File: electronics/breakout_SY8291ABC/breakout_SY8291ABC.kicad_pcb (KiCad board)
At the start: 2 copper layers, 18.5 x 12.7 mm, 19 parts, among them J1 Conn_01x04, U1 SY8120

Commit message: modified, layedout, and completed, now wait one day in between
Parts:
- removed C2: 10u, SquantorRcl:C_1206_0805
- C4: value 47p -> 22p
- L1: value 4.7u -> TBD
- N1: value 20210414 -> 20210417
- R3: value 22K -> TBD
- U1: value SY8120 -> SY8291
- moved R5 1.80 mm to (150.4, 75.6), turned to 180 degrees
- moved N1 0.95 mm to (148.8, 71.3)
- moved C1 0.90 mm to (144.2, 75.0)
- moved C3 0.90 mm to (147.7, 72.0)
- moved C4 0.90 mm to (141.0, 68.5)
- moved L1 0.90 mm to (151.8, 70.4)
- moved R2 0.90 mm to (142.1, 68.5)
- moved U1 0.90 mm to (145.2, 71.7)
- moved C5 0.90 mm to (145.5, 67.8)
- moved C6 0.90 mm to (143.6, 67.8)
- moved C7 0.90 mm to (147.4, 67.8)
- moved R1 0.90 mm to (141.7, 71.1)
- moved R3 0.90 mm to (142.8, 71.1)
- moved R4 0.90 mm to (140.6, 71.1)
- moved D1 0.82 mm to (153.1, 75.6), turned to 180 degrees
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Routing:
- net /Vin: track 23.4 -> 17.4 mm, vias 6 -> 7
- net /Vout: track 45.1 -> 47.5 mm
- net Net-(D1-Pad2): track 2.71 -> 1.30 mm
- net /GND: track 5.62 -> 6.57 mm
- net /Enable: track 4.62 -> 5.52 mm
- added copper zone on B.Cu, net /Vin
- added copper zone on F.Cu, net /Vin
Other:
- board size 18.5 x 12.7 mm -> 18.5 x 10.7 mm

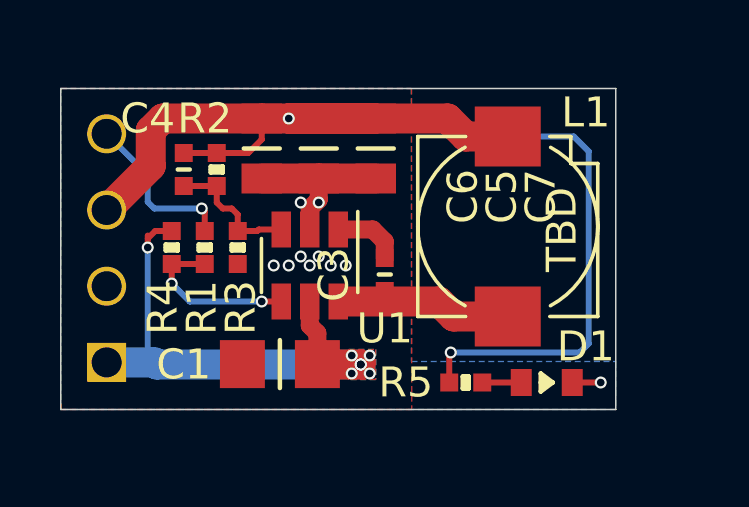
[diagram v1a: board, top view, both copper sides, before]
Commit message: added additional current label, optimized some track placement
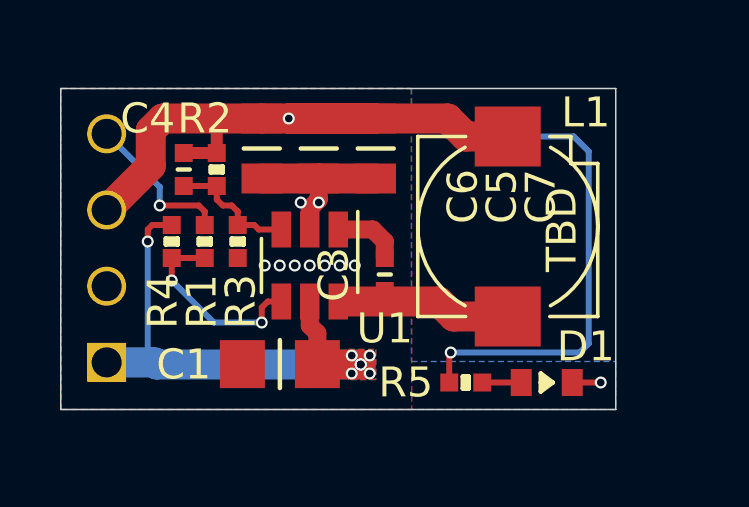
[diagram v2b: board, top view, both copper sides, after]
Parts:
- added N4: A:, SquantorLabels:Label_Note_medium, B.Cu at (150.1, 75.4)
- N1: value 20210417 -> 20210418
- N3: value Vout: -> V:
- moved N3 5.01 mm to (153.5, 69.4), turned to 270 degrees
- moved N2 1.27 mm to (144.1, 72.1)
- moved N1 1.10 mm to (147.7, 71.3)
- moved R1 0.20 mm to (141.7, 70.9)
- moved R3 0.20 mm to (142.8, 70.9)
- moved R4 0.20 mm to (140.6, 70.9)
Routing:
- net /Vout: track 47.5 -> 46.2 mm
- net Net-(R1-Pad1): track 5.65 -> 6.66 mm

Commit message: added soldermask keepout, DRC errors fixed, title added, changed Vout Iout labels
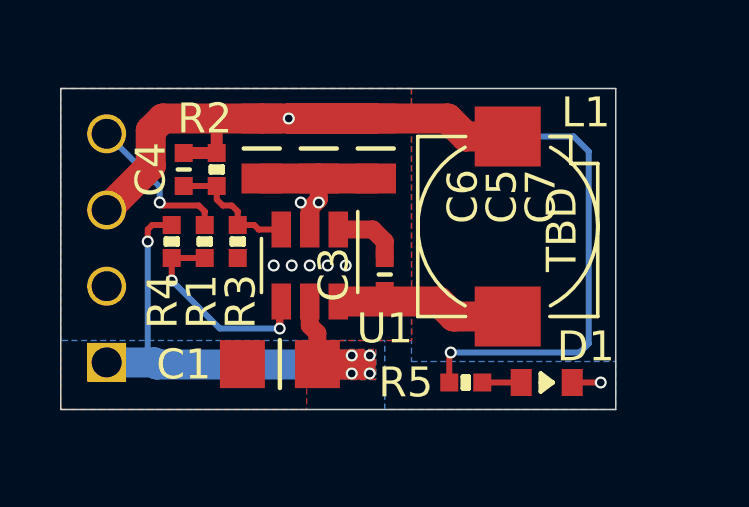
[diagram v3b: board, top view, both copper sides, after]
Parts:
- N1: value 20210418 -> 20210419
- moved N1 1.20 mm to (146.9, 70.4)
- moved N2 1.20 mm to (143.3, 71.2)
- moved N4 0.20 mm to (150.3, 75.4)
- moved N3 0.10 mm to (153.6, 69.4)
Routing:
- net /Vin: vias 7 -> 5
- net /GND: vias 10 -> 8
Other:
- board text added: "SY8291 40V 1.2A"

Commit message: changed indicator power led, changed inductor size, enlarged PCB a bit
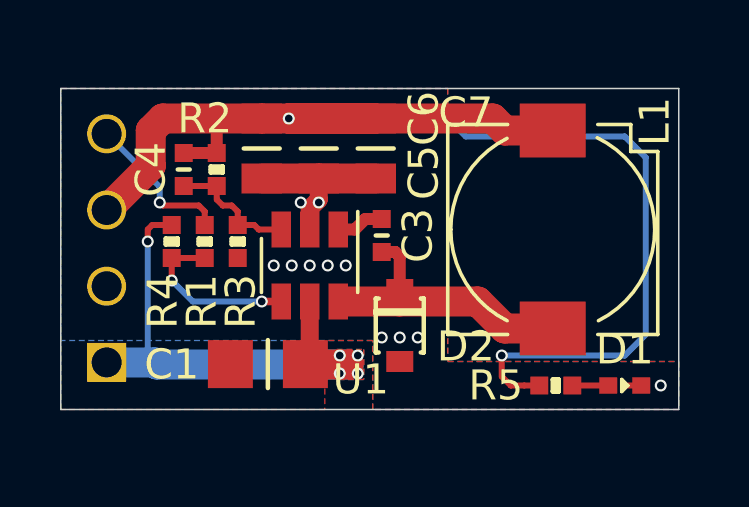
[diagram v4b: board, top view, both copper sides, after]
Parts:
- added D2: B140WS, SquantorDiodes:SOD_323_onsemi, F.Cu at (148.2, 73.7)
- D1: footprint SquantorDiodes:LED_0603_hand -> SquantorDiodes:LED_0402_osram
- L1: footprint SquantorRcl:L_SLF6045 -> SquantorRcl:L_SLF70XX_TDK_hand
- N1: value 20210419 -> 20210421
- moved R5 3.00 mm to (153.4, 75.7)
- moved D1 2.60 mm to (155.7, 75.7)
- moved L1 1.50 mm to (153.3, 70.5)
- moved C3 1.30 mm to (147.6, 70.7)
- moved C1 0.40 mm to (143.8, 75.0)
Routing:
- net /Vout: track 46.2 -> 50.5 mm
- net Net-(C3-Pad1): track 5.86 -> 9.68 mm
- net Net-(R1-Pad1): track 7.03 -> 5.79 mm
- net Net-(C3-Pad2): track 2.27 -> 1.59 mm
- net /GND: track 6.57 -> 6.27 mm, vias 8 -> 11
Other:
- board size 18.5 x 10.7 mm -> 20.6 x 10.7 mm

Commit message: updated versionnumber, changed coil sizes
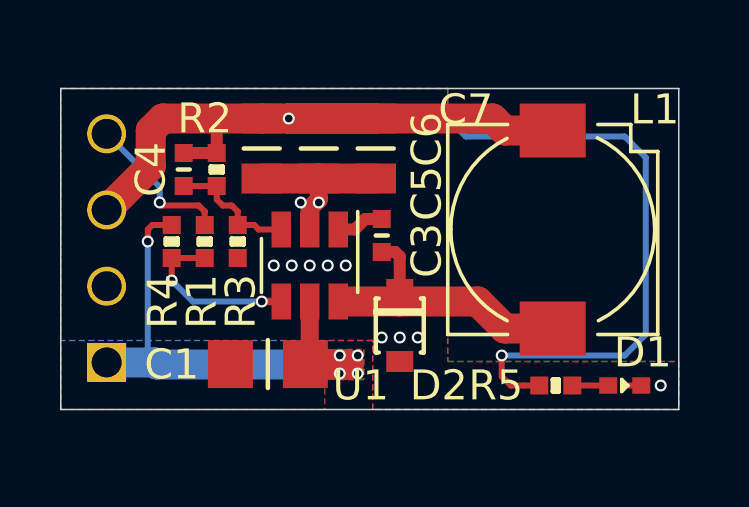
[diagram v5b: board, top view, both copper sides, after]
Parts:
- N1: value 20210421 -> 20210422
- moved N3 1.70 mm to (155.3, 69.4)
- moved N4 1.70 mm to (152.0, 75.4)
- moved N1 1.30 mm to (148.2, 70.4)
- moved N2 1.30 mm to (144.6, 71.2)

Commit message: minor silk updates, updated versionnumber
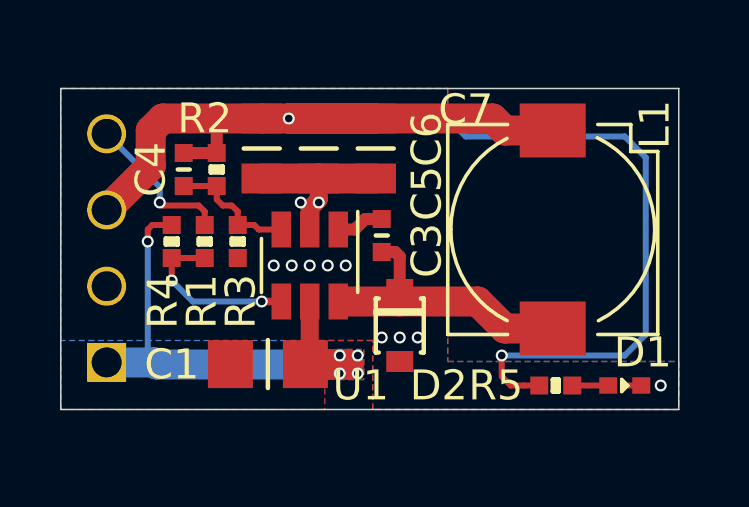
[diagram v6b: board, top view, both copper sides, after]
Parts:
- N1: value 20210422 -> 20210423
